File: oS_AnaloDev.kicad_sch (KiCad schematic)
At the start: 1 part, among them J1 Conn_02x15_Odd_Even

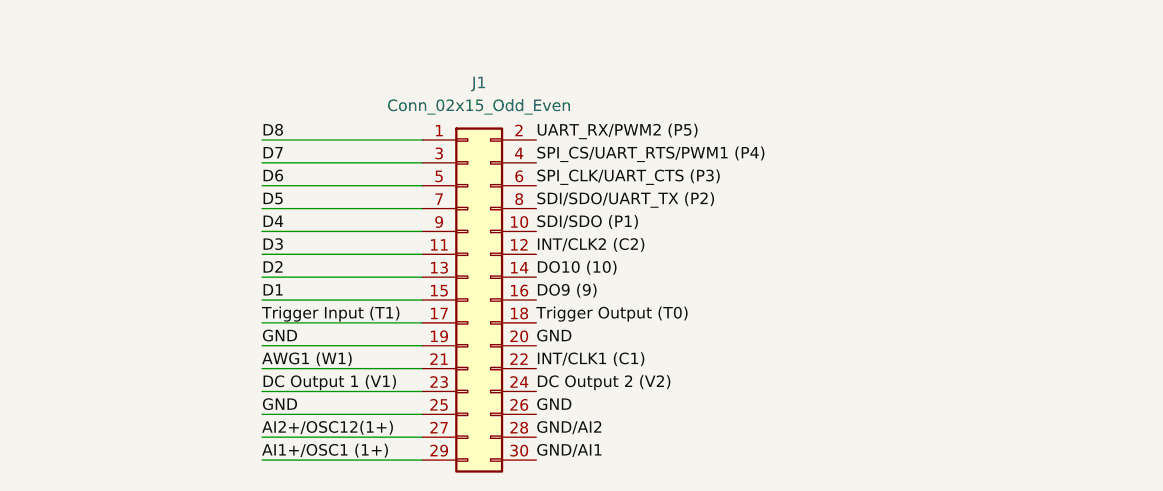
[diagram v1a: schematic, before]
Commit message: feat: agregar hierarchical_labels con nombres correctos a oS_AnaloDev (DiscoveryAnalog3) - 30 pines
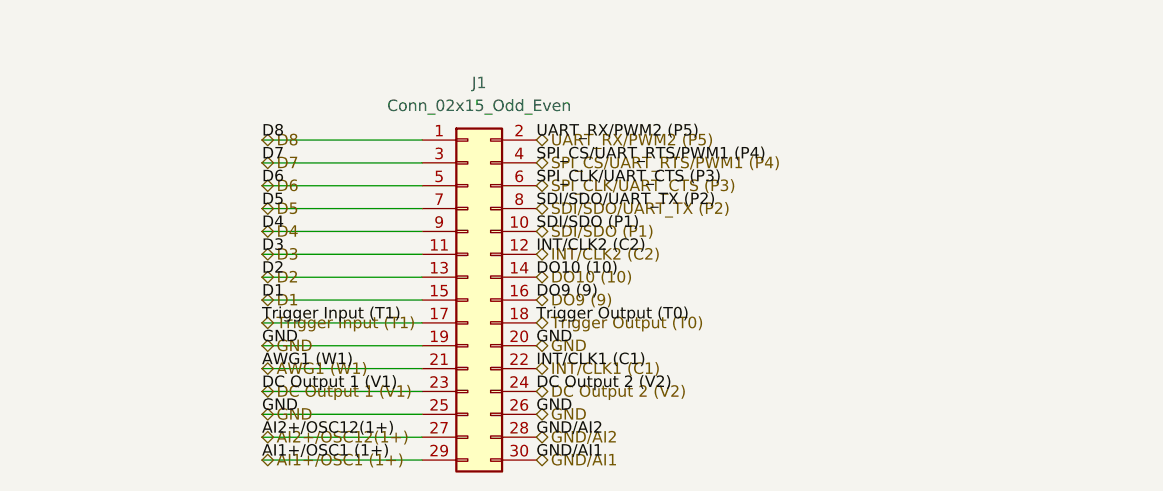
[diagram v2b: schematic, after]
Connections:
- net AI1+/OSC1 (1+) renamed AI1+/OSC1 (1+)
- net AI2+/OSC12(1+) renamed AI2+/OSC12(1+)
- net DC Output 2 (V2)  renamed DC Output 2 (V2)
- net DO10 (10)  renamed DO10 (10)
- net DO9 (9)  renamed DO9 (9)
- net GND/AI1 renamed GND/AI1
- net GND/AI2 renamed GND/AI2
- net INT/CLK1 (C1)  renamed INT/CLK1 (C1)
- net INT/CLK2 (C2)  renamed INT/CLK2 (C2)
- net SDI/SDO (P1)  renamed SDI/SDO (P1)
- net SDI/SDO/UART_TX (P2)  renamed SDI/SDO/UART_TX (P2)
- net SPI_CLK/UART_CTS (P3)  renamed SPI_CLK/UART_CTS (P3)
- net SPI_CS/UART_RTS/PWM1 (P4) renamed SPI_CS/UART_RTS/PWM1 (P4)
- net Trigger Output (T0)  renamed Trigger Output (T0)
- net UART_RX/PWM2 (P5) renamed UART_RX/PWM2 (P5)

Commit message: feat: PIM100 - labels en mayusculas y pines externos ordenados por puerto (85 pines, 42 izq + 43 der)
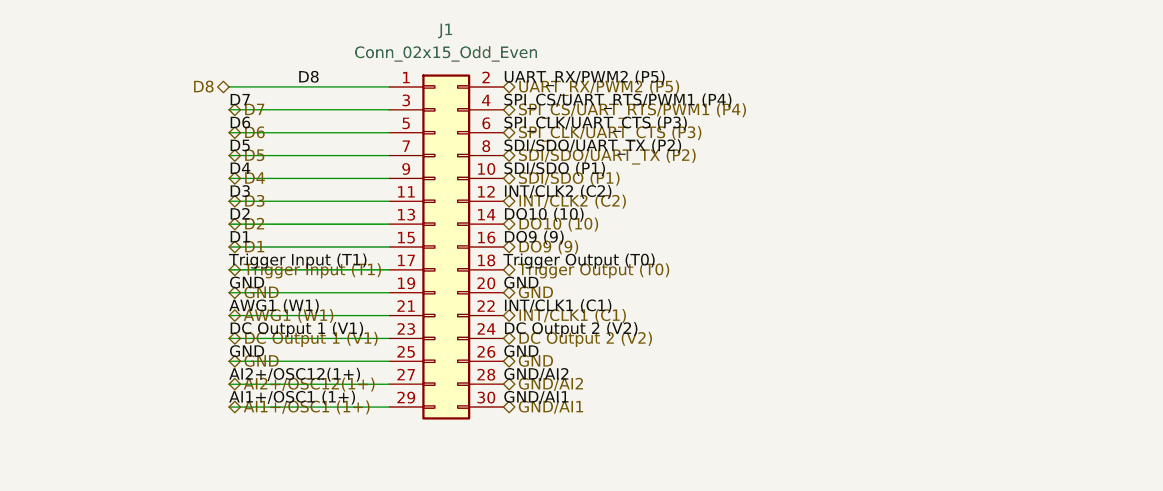
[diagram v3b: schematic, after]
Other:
- moved on the sheet: J1

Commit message: feat: agregar 31 pines jerarquicos al sheet pic18F46j50 - ordenados por puerto (15 izq + 16 der)
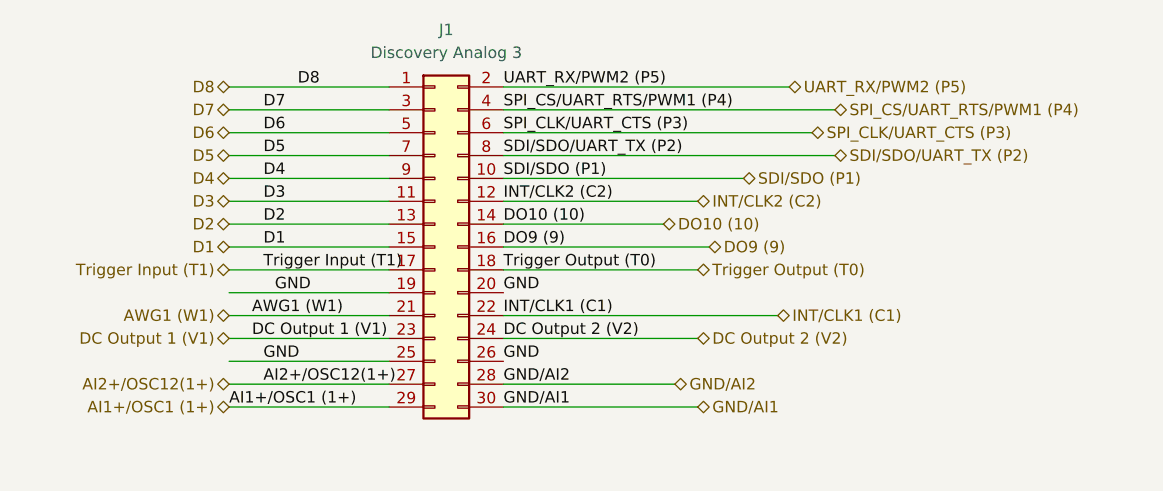
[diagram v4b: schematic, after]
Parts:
- J1: value Conn_02x15_Odd_Even -> Discovery Analog 3
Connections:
- net AI1+/OSC1 (1+) renamed AI1+/OSC1 (1+)
- net AI2+/OSC12(1+) renamed AI2+/OSC12(1+)
- net GND/AI1 renamed GND/AI1
- net GND/AI2 renamed GND/AI2
- net INT/CLK1 (C1) renamed INT/CLK1 (C1)
- net INT/CLK2 (C2) renamed INT/CLK2 (C2)
- net SDI/SDO (P1) renamed SDI/SDO (P1)
- net SDI/SDO/UART_TX (P2) renamed SDI/SDO/UART_TX (P2)
- net SPI_CLK/UART_CTS (P3) renamed SPI_CLK/UART_CTS (P3)
- net SPI_CS/UART_RTS/PWM1 (P4) renamed SPI_CS/UART_RTS/PWM1 (P4)
- net UART_RX/PWM2 (P5) renamed UART_RX/PWM2 (P5)
